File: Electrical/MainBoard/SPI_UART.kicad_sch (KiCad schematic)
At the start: 7 parts, among them J18 Conn_02x02_Odd_Even, J19 Conn_02x03_Odd_Even, J20 Conn_01x06, J22 Conn_02x02_Odd_Even, J23 Conn_02x03_Odd_Even, J27 Conn_01x06_Socket, J8 Conn_02x04_Odd_Even

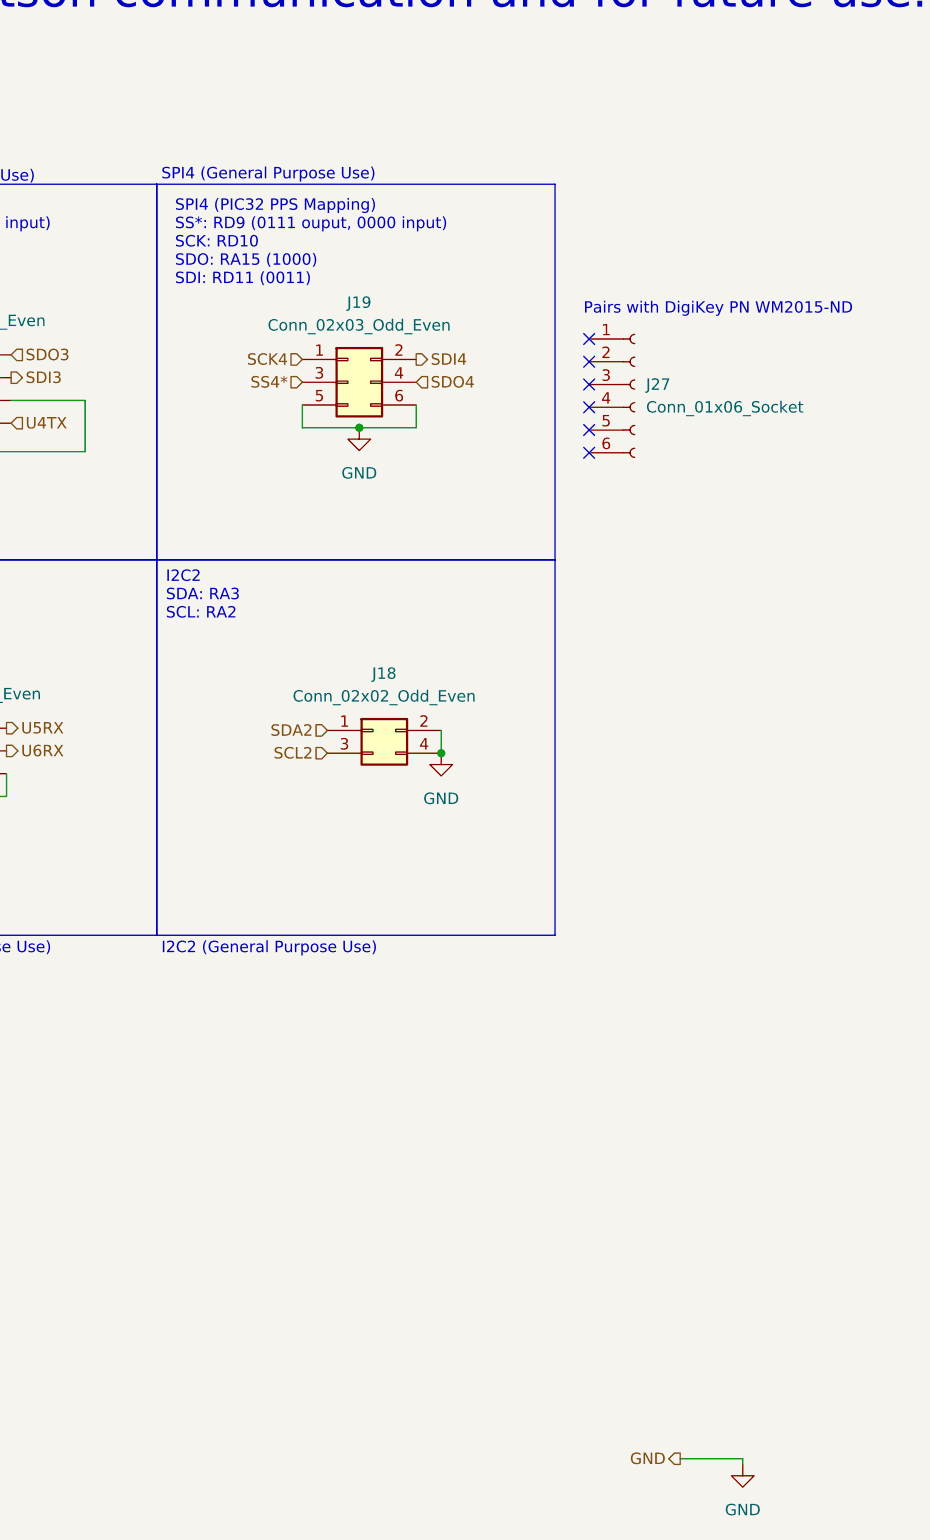
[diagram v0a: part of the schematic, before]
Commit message: Change some connections to picoblade, add env sensor connector
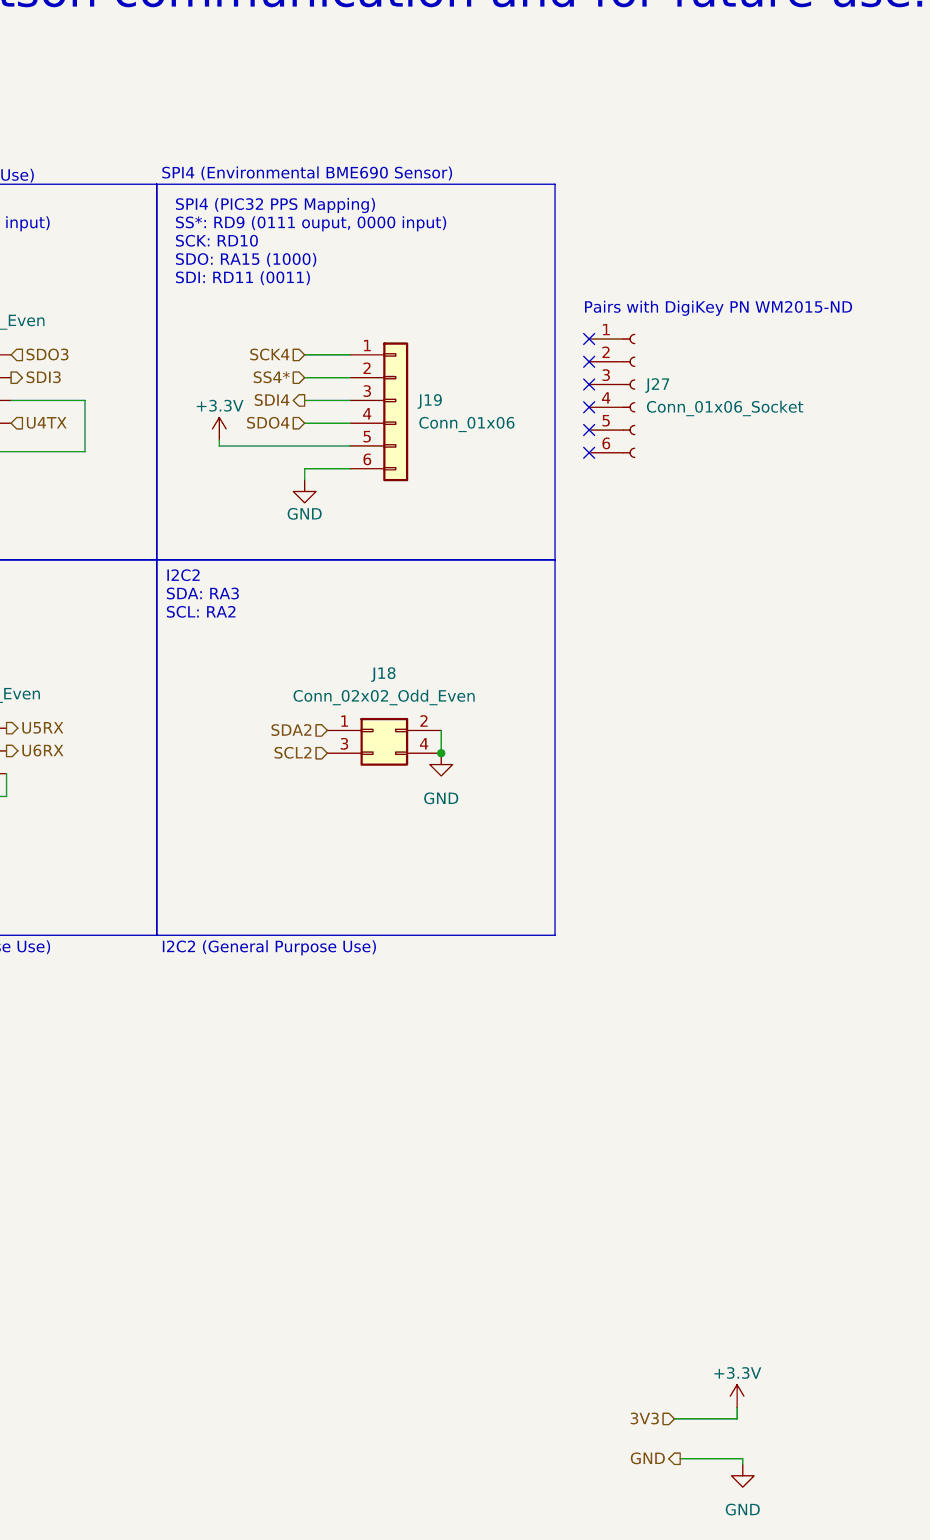
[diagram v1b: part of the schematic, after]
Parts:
- removed J19: Conn_02x03_Odd_Even, Connector_PinHeader_2.54mm:PinHeader_2x03_P2.54mm_Vertical, symbol Connector_Generic:Conn_02x03_Odd_Even
- added J19: Conn_01x06, Connector_Molex:Molex_PicoBlade_53047-0610_1x06_P1.25mm_Vertical, symbol Connector_Generic:Conn_01x06
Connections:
- net GND: now also J19.6 (Pin_6)
- net SCK4: now also J19.1 (Pin_1)
- net SDI4: now also J19.3 (Pin_3)
- net SDO4: now also J19.4 (Pin_4)
- net SS4*: now also J19.2 (Pin_2)
- new net +3.3V: J19.5 (Pin_5)
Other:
- note added: "SPI4 (Environmental BME690 Sensor)"
- note removed: "SPI4 (General Purpose Use)"

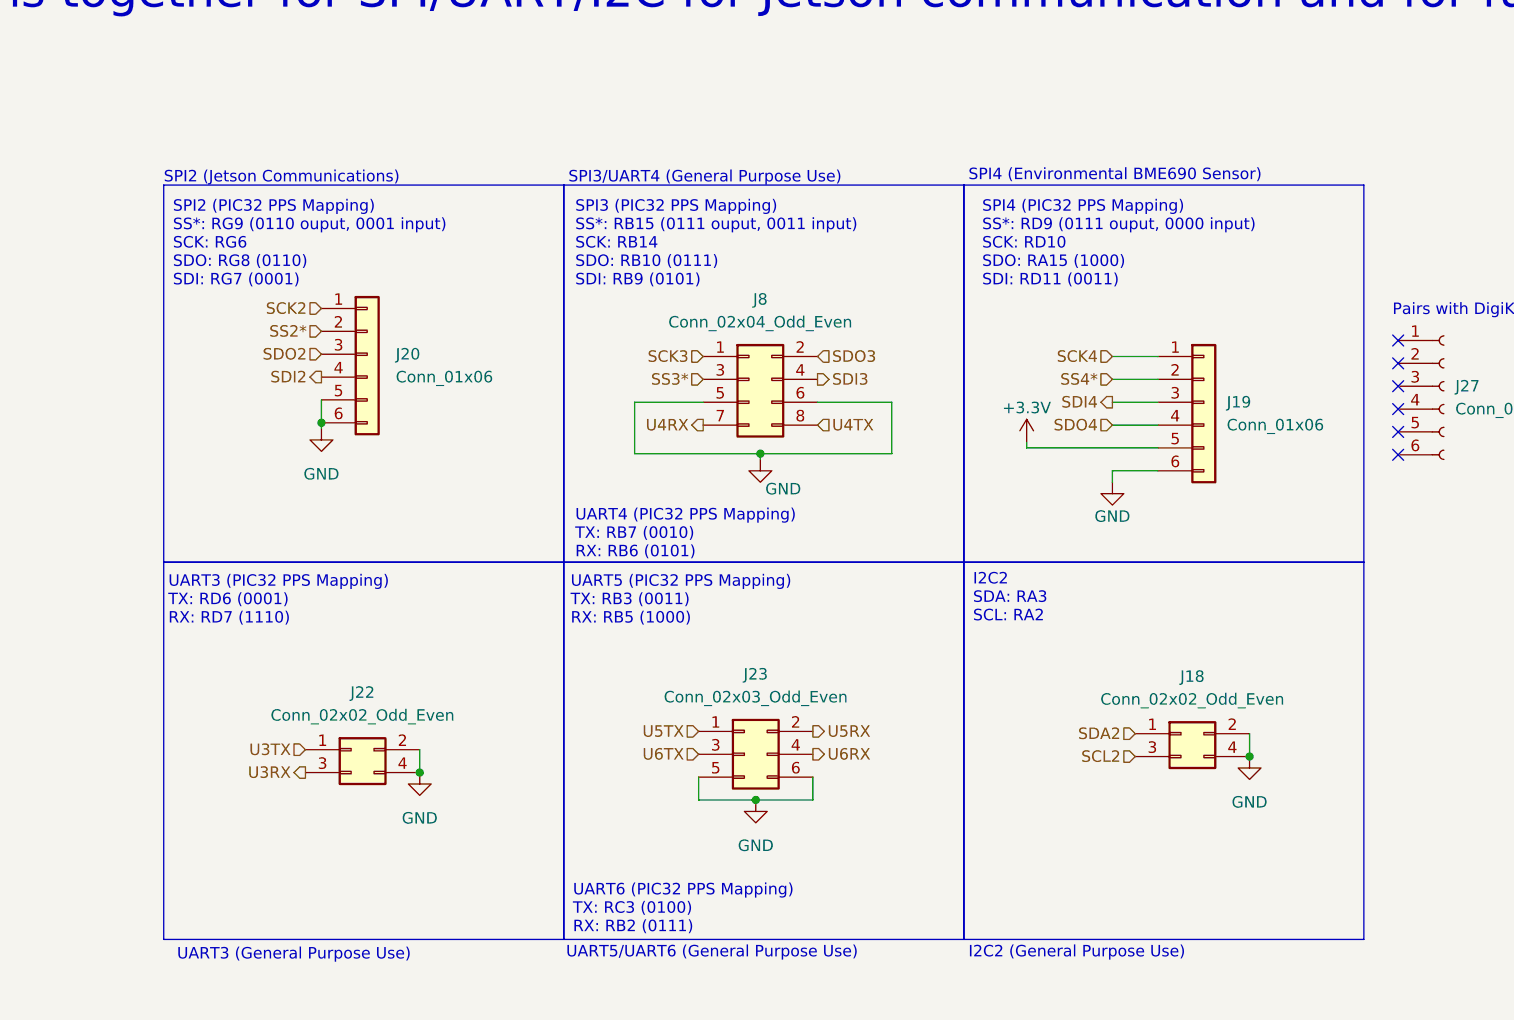
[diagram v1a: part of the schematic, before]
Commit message: Use more molex picoblades and make schematic prettier
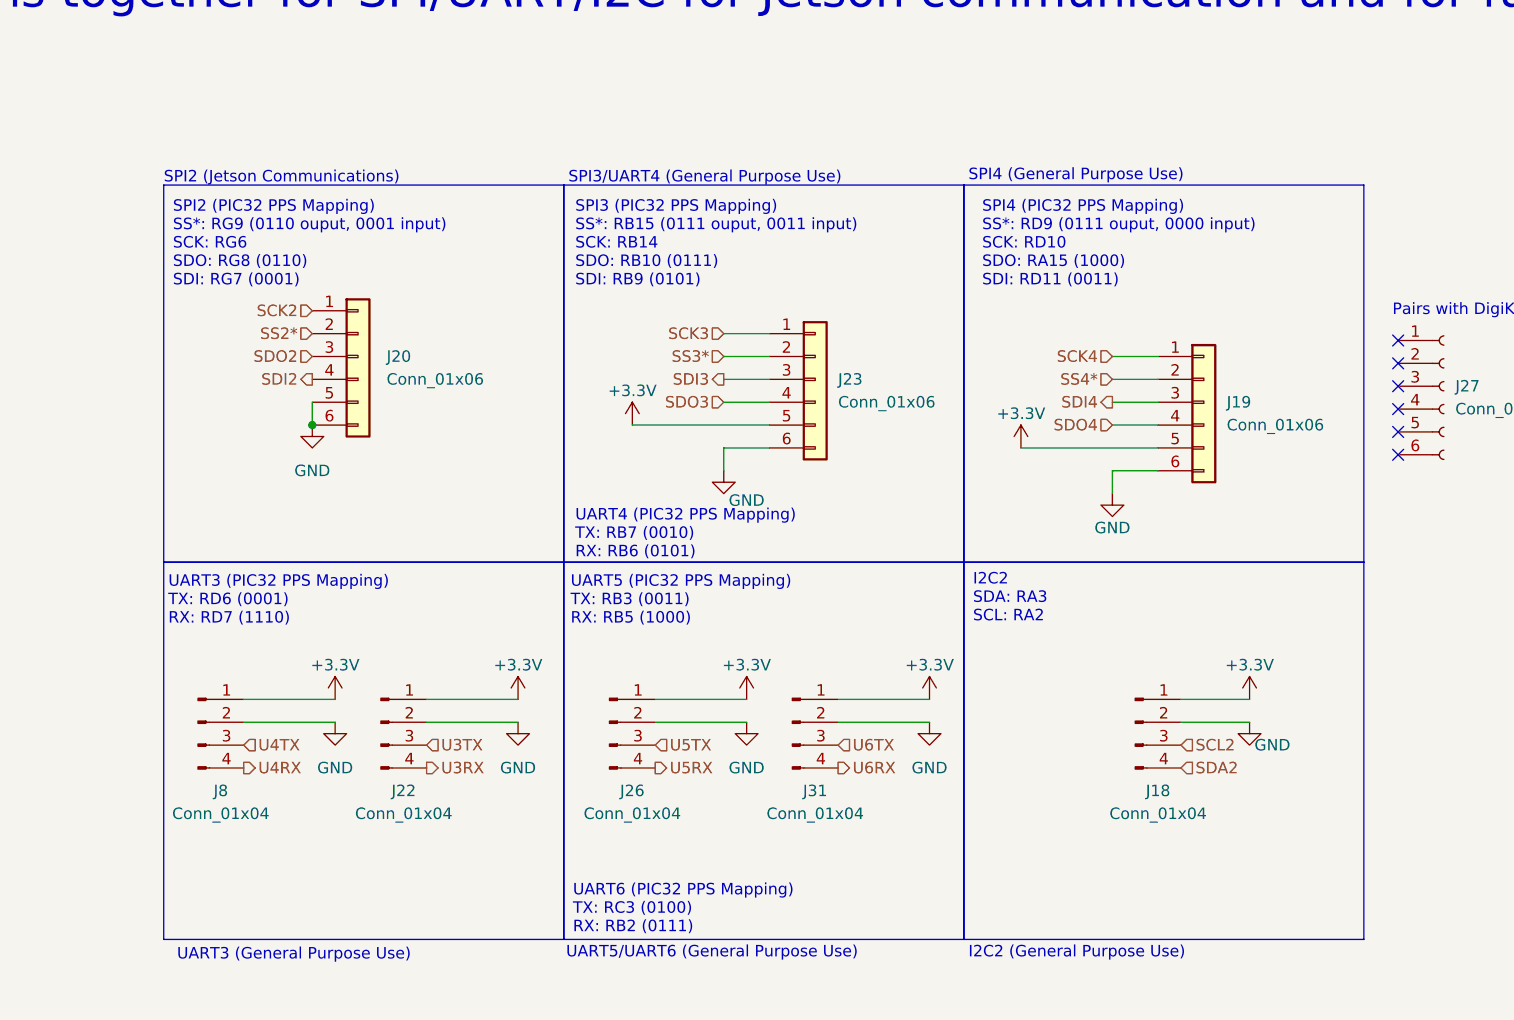
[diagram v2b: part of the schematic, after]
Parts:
- removed J22: Conn_02x02_Odd_Even, Connector_PinHeader_2.54mm:PinHeader_2x02_P2.54mm_Vertical, symbol Connector_Generic:Conn_02x02_Odd_Even
- removed J23: Conn_02x03_Odd_Even, Connector_PinHeader_2.54mm:PinHeader_2x03_P2.54mm_Vertical, symbol Connector_Generic:Conn_02x03_Odd_Even
- removed J8: Conn_02x04_Odd_Even, Connector_PinHeader_2.54mm:PinHeader_2x04_P2.54mm_Vertical, symbol Connector_Generic:Conn_02x04_Odd_Even
- added J22, J26, J31, J8: Conn_01x04, Connector_Molex:Molex_PicoBlade_53047-0410_1x04_P1.25mm_Vertical, symbol Connector:Conn_01x04_Pin
- added J23: Conn_01x06, Connector_Molex:Molex_PicoBlade_53047-0610_1x06_P1.25mm_Vertical, symbol Connector_Generic:Conn_01x06
- J18: value Conn_02x02_Odd_Even -> Conn_01x04; footprint Connector_PinHeader_2.54mm:PinHeader_2x02_P2.54mm_Vertical -> Connector_Molex:Molex_PicoBlade_53047-0410_1x04_P1.25mm_Vertical; symbol Connector_Generic:Conn_02x02_Odd_Even -> Connector:Conn_01x04_Pin; Mfr Amphenol ICC (FCI) -> Molex; Mfr P/N 10129381-904003BLF -> 0530470410; Supplier 1 P/N 10129381-904003BLF-ND -> WM1733-ND; now in the parts list
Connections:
- net +3.3V: now also J18.1 (Pin_1), J22.1 (Pin_1), J23.5 (Pin_5), J26.1 (Pin_1), J31.1 (Pin_1), J8.1 (Pin_1)
- net GND: now also J22.2 (Pin_2), J23.6 (Pin_6), J26.2 (Pin_2), J31.2 (Pin_2), J8.2 (Pin_2); no longer J18.4 (Pin_4)
- net SCK3: now also J23.1 (Pin_1)
- net SDA2: now also J18.4 (Pin_4); no longer J18.1 (Pin_1)
- net SDI3: now also J23.3 (Pin_3)
- net SDO3: now also J23.4 (Pin_4)
- net SS3*: now also J23.2 (Pin_2)
- net U3RX: now also J22.4 (Pin_4)
- net U3TX: now also J22.3 (Pin_3)
- net U4RX: now also J8.4 (Pin_4)
- net U4TX: now also J8.3 (Pin_3)
- net U5RX: now also J26.4 (Pin_4)
- net U5TX: now also J26.3 (Pin_3)
- net U6RX: now also J31.4 (Pin_4)
- net U6TX: now also J31.3 (Pin_3)
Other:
- note added: "SPI4 (General Purpose Use)"
- note removed: "SPI4 (Environmental BME690 Sensor)"
- moved on the sheet: J20

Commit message: Finalize updated schematics
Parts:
- J19, J22, J23, J26, J31, J8: now left out of the parts list
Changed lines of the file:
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@@
 		(unit 1)
 		(exclude_from_sim no)
-		(in_bom yes)
+		(in_bom no)
 		(on_board yes)
 		(dnp no)
@@
 		(unit 1)
 		(exclude_from_sim no)
-		(in_bom yes)
+		(in_bom no)
 		(on_board yes)
 		(dnp no)
@@
 		(unit 1)
 		(exclude_from_sim no)
-		(in_bom yes)
+		(in_bom no)
 		(on_board yes)
 		(dnp no)
@@
 		(unit 1)
 		(exclude_from_sim no)
-		(in_bom yes)
+		(in_bom no)
 		(on_board yes)
 		(dnp no)
@@
 		(unit 1)
 		(exclude_from_sim no)
-		(in_bom yes)
+		(in_bom no)
 		(on_board yes)
 		(dnp no)
@@
 		(unit 1)
 		(exclude_from_sim no)
-		(in_bom yes)
-		(on_board yes)
-		(dnp no)
+		(in_bom no)
+		(on_board yes)
+		(dnp no)
